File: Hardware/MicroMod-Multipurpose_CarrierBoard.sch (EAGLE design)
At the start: 83 parts, among them J11 microSD, J12 SPI, J14 I2C, J3 JTAG, J5 UART, J6 MICROMOD-2222-C, J8 Dedicated, Q2 600mA/40V, U1 S25FL127SABMFI100, U2 MCP73831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

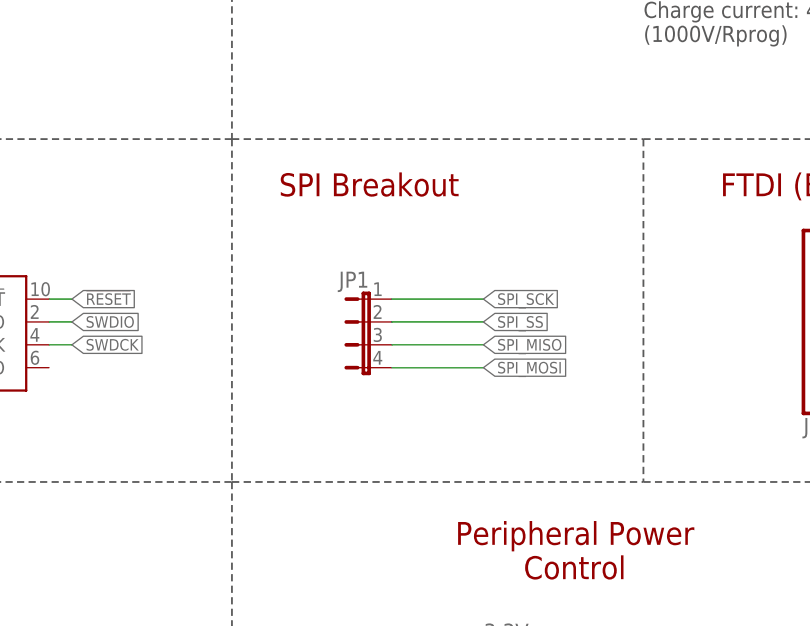
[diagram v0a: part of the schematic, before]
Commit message: FIX: Flash memory SPI breakout
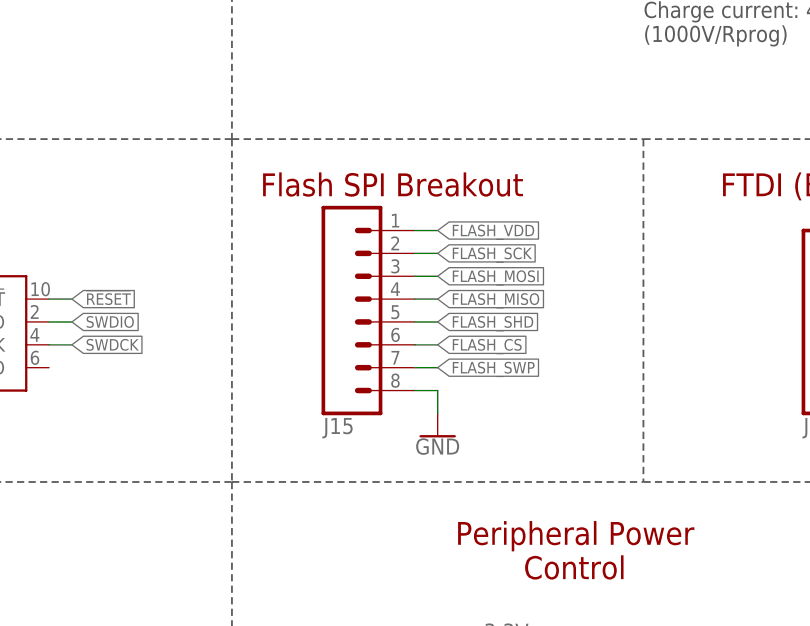
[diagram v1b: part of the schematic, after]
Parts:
- removed JP1: (no value), jumper:JP4E
- added J15: (no value), SparkFun-Connectors:CONN_08"
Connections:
- removed net SPI_MISO: JP1.3
- removed net SPI_MOSI: JP1.4
- removed net SPI_SS: JP1.2
- net FLASH_CS: now also J15.6
- net FLASH_MISO: now also J15.4
- net FLASH_MOSI: now also J15.3
- net FLASH_SCK: now also J15.2
- net FLASH_SHD: now also J15.5
- net FLASH_SWP: now also J15.7
- net FLASH_VDD: now also J15.1
- net GND: now also J15.8
- net SPI_SCK: no longer JP1.1
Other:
- note added: "Flash SPI Breakout"
- note removed: "SPI Breakout"
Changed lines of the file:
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@@
 <part name="GND1" library="SparkFun-PowerSymbols" deviceset="GND" device=""/>
 <part name="GND2" library="SparkFun-PowerSymbols" deviceset="GND" device=""/>
-<part name="JP1" library="jumper" library_urn="urn:adsk.eagle:library:252" deviceset="JP4E" device="" package3d_urn="urn:adsk.eagle:package:15463/1"/>
 <part name="J2" library="SparkFun-Connectors" library_urn="urn:adsk.eagle:library:513" deviceset="CONN_07" device="" package3d_urn="urn:adsk.eagle:package:38129/1"/>
 <part name="GND5" library="SparkFun-PowerSymbols" deviceset="GND" device=""/>
@@
 <part name="H3" library="SparkFun-Hardware" library_urn="urn:adsk.eagle:library:519" deviceset="STAND-OFF" device="" package3d_urn="urn:adsk.eagle:package:38630/1"/>
 <part name="H4" library="SparkFun-Hardware" library_urn="urn:adsk.eagle:library:519" deviceset="STAND-OFF" device="" package3d_urn="urn:adsk.eagle:package:38630/1"/>
+<part name="J15" library="SparkFun-Connectors" library_urn="urn:adsk.eagle:library:513" deviceset="CONN_08" device="&quot;" package3d_urn="urn:adsk.eagle:package:38138/1"/>
+<part name="GND36" library="SparkFun-PowerSymbols" deviceset="GND" device=""/>
 </parts>
 <sheets>
@@
 <wire x1="287.02" y1="0" x2="289.56" y2="0" width="0.2" layer="97" style="longdash"/>
 <wire x1="287.02" y1="144.78" x2="332.74" y2="144.78" width="0.2032" layer="97" style="longdash"/>
-<text x="302.26" y="139.7" size="2.54" layer="94" align="center">SPI Breakout</text>
+<text x="304.8" y="139.7" size="2.54" layer="94" align="center">Flash SPI Breakout</text>
 <wire x1="287.02" y1="106.68" x2="332.74" y2="106.68" width="0.2032" layer="97" style="longdash"/>
 <text x="325.12" y="99.06" size="2.54" layer="94" align="center">Peripheral Power
@@
 <attribute name="VALUE" x="35.56" y="131.826" size="1.778" layer="96" align="top-center"/>
 </instance>
-<instance part="JP1" gate="G$1" x="302.26" y="124.46" smashed="yes" rot="MR270">
-<attribute name="NAME" x="302.26" y="128.27" size="1.778" layer="95" rot="MR0"/>
-<attribute name="VALUE" x="302.26" y="116.205" size="1.778" layer="96" rot="MR0"/>
-</instance>
 <instance part="J2" gate="G$1" x="355.6" y="127" smashed="yes" rot="MR180">
 <attribute name="VALUE" x="350.52" y="136.906" size="1.778" layer="96" font="vector" rot="MR180"/>
@@
 <instance part="H3" gate="G$1" x="411.48" y="25.4" smashed="yes"/>
 <instance part="H4" gate="G$1" x="408.94" y="25.4" smashed="yes"/>
+<instance part="J15" gate="G$1" x="302.26" y="127" smashed="yes" rot="MR180">
+<attribute name="VALUE" x="297.18" y="139.446" size="1.778" layer="96" font="vector" rot="MR180"/>
+<attribute name="NAME" x="297.18" y="113.792" size="1.778" layer="95" font="vector" rot="MR180"/>
+</instance>
+<instance part="GND36" gate="1" x="309.88" y="111.76" smashed="yes" rot="MR0">
+<attribute name="VALUE" x="309.88" y="111.506" size="1.778" layer="96" rot="MR0" align="top-center"/>
+</instance>
 </instances>
 <busses>
@@
 <wire x1="243.84" y1="119.38" x2="241.3" y2="119.38" width="0.1524" layer="91"/>
 <pinref part="J3" gate="G$1" pin="GND"/>
+</segment>
+<segment>
+<pinref part="J15" gate="G$1" pin="8"/>
+<wire x1="307.34" y1="116.84" x2="309.88" y2="116.84" width="0.1524" layer="91"/>
+<pinref part="GND36" gate="1" pin="GND"/>
+<wire x1="309.88" y1="116.84" x2="309.88" y2="114.3" width="0.1524" layer="91"/>
 </segment>
 </net>
@@
 </segment>
 <segment>
-<pinref part="JP1" gate="G$1" pin="1"/>
-<wire x1="304.8" y1="127" x2="314.96" y2="127" width="0.1524" layer="91"/>
-<label x="314.96" y="127" size="1.27" layer="95" font="vector" xref="yes"/>
-</segment>
-<segment>
 <pinref part="J6" gate="J1" pin="SPI_SCK"/>
 <wire x1="208.28" y1="93.98" x2="210.82" y2="93.98" width="0.1524" layer="91"/>
@@
 <label x="210.82" y="25.4" size="1.27" layer="95" font="vector" xref="yes"/>
 </segment>
+<segment>
+<pinref part="J15" gate="G$1" pin="7"/>
+<wire x1="307.34" y1="119.38" x2="309.88" y2="119.38" width="0.1524" layer="91"/>
+<label x="309.88" y="119.38" size="1.27" layer="95" font="vector" xref="yes"/>
+</segment>
 </net>
 <net name="FLASH_SHD" class="0">
@@
 <wire x1="208.28" y1="27.94" x2="210.82" y2="27.94" width="0.1524" layer="91"/>
 <label x="210.82" y="27.94" size="1.27" layer="95" font="vector" xref="yes"/>
+</segment>
+<segment>
+<pinref part="J15" gate="G$1" pin="5"/>
+<wire x1="307.34" y1="124.46" x2="309.88" y2="124.46" width="0.1524" layer="91"/>
+<label x="309.88" y="124.46" size="1.27" layer="95" font="vector" xref="yes"/>
 </segment>
 </net>
@@
 <label x="383.54" y="254" size="1.27" layer="95" font="vector" xref="yes"/>
 </segment>
-</net>
-<net name="SPI_SS" class="0">
-<segment>
-<pinref part="JP1" gate="G$1" pin="2"/>
-<wire x1="304.8" y1="124.46" x2="314.96" y2="124.46" width="0.1524" layer="91"/>
-<label x="314.96" y="124.46" size="1.27" layer="95" font="vector" xref="yes"/>
-</segment>
-</net>
-<net name="SPI_MISO" class="0">
-<segment>
-<pinref part="JP1" gate="G$1" pin="3"/>
-<wire x1="304.8" y1="121.92" x2="314.96" y2="121.92" width="0.1524" layer="91"/>
-<label x="314.96" y="121.92" size="1.27" layer="95" font="vector" xref="yes"/>
-</segment>
-</net>
-<net name="SPI_MOSI" class="0">
-<segment>
-<pinref part="JP1" gate="G$1" pin="4"/>
-<wire x1="304.8" y1="119.38" x2="314.96" y2="119.38" width="0.1524" layer="91"/>
-<label x="314.96" y="119.38" size="1.27" layer="95" font="vector" xref="yes"/>
+<segment>
+<pinref part="J15" gate="G$1" pin="1"/>
+<wire x1="307.34" y1="134.62" x2="309.88" y2="134.62" width="0.1524" layer="91"/>
+<label x="309.88" y="134.62" size="1.27" layer="95" font="vector" xref="yes"/>
 </segment>
 </net>
@@
 <wire x1="208.28" y1="99.06" x2="210.82" y2="99.06" width="0.1524" layer="91"/>
 <label x="210.82" y="99.06" size="1.27" layer="95" font="vector" xref="yes"/>
+</segment>
+<segment>
+<pinref part="J15" gate="G$1" pin="6"/>
+<wire x1="307.34" y1="121.92" x2="309.88" y2="121.92" width="0.1524" layer="91"/>
+<label x="309.88" y="121.92" size="1.27" layer="95" font="vector" xref="yes"/>
 </segment>
 </net>
@@
 <label x="210.82" y="111.76" size="1.27" layer="95" font="vector" xref="yes"/>
 </segment>
+<segment>
+<pinref part="J15" gate="G$1" pin="2"/>
+<wire x1="307.34" y1="132.08" x2="309.88" y2="132.08" width="0.1524" layer="91"/>
+<label x="309.88" y="132.08" size="1.27" layer="95" font="vector" xref="yes"/>
+</segment>
 </net>
 <net name="FLASH_MOSI" class="0">
@@
 <wire x1="208.28" y1="109.22" x2="210.82" y2="109.22" width="0.1524" layer="91"/>
 <label x="210.82" y="109.22" size="1.27" layer="95" font="vector" xref="yes"/>
+</segment>
+<segment>
+<pinref part="J15" gate="G$1" pin="3"/>
+<wire x1="307.34" y1="129.54" x2="309.88" y2="129.54" width="0.1524" layer="91"/>
+<label x="309.88" y="129.54" size="1.27" layer="95" font="vector" xref="yes"/>
 </segment>
 </net>
@@
 <label x="210.82" y="106.68" size="1.27" layer="95" font="vector" xref="yes"/>
 </segment>
-</net>
+<segment>
+<pinref part="J15" gate="G$1" pin="4"/>
+<wire x1="307.34" y1="127" x2="309.88" y2="127" width="0.1524" layer="91"/>
+<label x="309.88" y="127" size="1.27" layer="95" font="vector" xref="yes"/>
+</segment>
+</net>

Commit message: Wire I2C_SCL1/SDA1 and G4-G11 as breakout GPIO pins
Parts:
- added J16: General GPIO, SparkFun-Connectors:CONN_08"
- added J17: I2C1, SparkFun-Connectors:I2C_STANDARD_NO_SILK
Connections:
- new net G10: J16.7, J6.G10/ADC_D+/CAM_VSYNC
- new net G11: J16.8, J6.G11
- new net G4: J16.1, J6.G4/BUS4
- new net G5: J16.2, J6.G5/BUS5
- new net G6: J16.3, J6.G6/BUS6
- new net G7: J16.4, J6.G7/BUS7
- new net G8: J16.5, J6.G8
- new net G9: J16.6, J6.G9/ADC_D-/CAM_HSYNC
- new net I2C_SCL1: J17.4, J6.I2C_SCL1
- new net I2C_SDA1: J17.3, J6.I2C_SDA1
- net 3.3V_LP: now also J17.2
- net FLASH_SHD: now also J6.G2/BUS2; no longer J6.G7/BUS7
- net FLASH_SWP: now also J6.G3/BUS3; no longer J6.G8
- net GND: now also J17.1
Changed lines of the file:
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@@
 <part name="J15" library="SparkFun-Connectors" library_urn="urn:adsk.eagle:library:513" deviceset="CONN_08" device="&quot;" package3d_urn="urn:adsk.eagle:package:38138/1"/>
 <part name="GND36" library="SparkFun-PowerSymbols" deviceset="GND" device=""/>
+<part name="J16" library="SparkFun-Connectors" library_urn="urn:adsk.eagle:library:513" deviceset="CONN_08" device="&quot;" package3d_urn="urn:adsk.eagle:package:38138/1" value="General GPIO"/>
+<part name="J17" library="SparkFun-Connectors" deviceset="I2C_STANDARD" device="_NO_SILK" value="I2C1"/>
+<part name="GND37" library="SparkFun-PowerSymbols" deviceset="GND" device=""/>
 </parts>
 <sheets>
@@
 <attribute name="VALUE" x="309.88" y="111.506" size="1.778" layer="96" rot="MR0" align="top-center"/>
 </instance>
+<instance part="J16" gate="G$1" x="78.74" y="78.74" smashed="yes" rot="MR180">
+<attribute name="VALUE" x="73.66" y="91.186" size="1.778" layer="96" font="vector" rot="MR180"/>
+<attribute name="NAME" x="73.66" y="65.532" size="1.778" layer="95" font="vector" rot="MR180"/>
+</instance>
+<instance part="J17" gate="G$1" x="109.22" y="12.7" smashed="yes" rot="MR0">
+<attribute name="VALUE" x="108.458" y="20.828" size="1.778" layer="96" font="vector" rot="MR180" align="top-left"/>
+<attribute name="NAME" x="107.95" y="5.334" size="1.778" layer="95" font="vector"/>
+</instance>
+<instance part="GND37" gate="1" x="99.06" y="5.08" smashed="yes">
+<attribute name="VALUE" x="99.06" y="4.826" size="1.778" layer="96" align="top-center"/>
+</instance>
 </instances>
 <busses>
@@
 <pinref part="GND36" gate="1" pin="GND"/>
 <wire x1="309.88" y1="116.84" x2="309.88" y2="114.3" width="0.1524" layer="91"/>
+</segment>
+<segment>
+<pinref part="J17" gate="G$1" pin="1"/>
+<wire x1="101.6" y1="10.16" x2="99.06" y2="10.16" width="0.1524" layer="91"/>
+<pinref part="GND37" gate="1" pin="GND"/>
+<wire x1="99.06" y1="10.16" x2="99.06" y2="7.62" width="0.1524" layer="91"/>
 </segment>
 </net>
@@
 <label x="45.72" y="48.26" size="1.27" layer="95" rot="R90" xref="yes"/>
 </segment>
+<segment>
+<pinref part="J17" gate="G$1" pin="2"/>
+<wire x1="101.6" y1="12.7" x2="99.06" y2="12.7" width="0.1524" layer="91"/>
+<wire x1="99.06" y1="12.7" x2="99.06" y2="20.32" width="0.1524" layer="91"/>
+<label x="99.06" y="20.32" size="1.27" layer="95" rot="R90" xref="yes"/>
+</segment>
 </net>
 <net name="FLASH_SWP" class="0">
@@
 </segment>
 <segment>
-<pinref part="J6" gate="J1" pin="G8"/>
-<wire x1="208.28" y1="25.4" x2="210.82" y2="25.4" width="0.1524" layer="91"/>
-<label x="210.82" y="25.4" size="1.27" layer="95" font="vector" xref="yes"/>
-</segment>
-<segment>
 <pinref part="J15" gate="G$1" pin="7"/>
 <wire x1="307.34" y1="119.38" x2="309.88" y2="119.38" width="0.1524" layer="91"/>
 <label x="309.88" y="119.38" size="1.27" layer="95" font="vector" xref="yes"/>
 </segment>
+<segment>
+<pinref part="J6" gate="J1" pin="G3/BUS3"/>
+<wire x1="208.28" y1="38.1" x2="210.82" y2="38.1" width="0.1524" layer="91"/>
+<label x="210.82" y="38.1" size="1.27" layer="95" font="vector" xref="yes"/>
+</segment>
 </net>
 <net name="FLASH_SHD" class="0">
@@
 </segment>
 <segment>
-<pinref part="J6" gate="J1" pin="G7/BUS7"/>
-<wire x1="208.28" y1="27.94" x2="210.82" y2="27.94" width="0.1524" layer="91"/>
-<label x="210.82" y="27.94" size="1.27" layer="95" font="vector" xref="yes"/>
-</segment>
-<segment>
 <pinref part="J15" gate="G$1" pin="5"/>
 <wire x1="307.34" y1="124.46" x2="309.88" y2="124.46" width="0.1524" layer="91"/>
 <label x="309.88" y="124.46" size="1.27" layer="95" font="vector" xref="yes"/>
+</segment>
+<segment>
+<pinref part="J6" gate="J1" pin="G2/BUS2"/>
+<wire x1="208.28" y1="40.64" x2="210.82" y2="40.64" width="0.1524" layer="91"/>
+<label x="210.82" y="40.64" size="1.27" layer="95" font="vector" xref="yes"/>
 </segment>
 </net>
@@
 </segment>
 </net>
+<net name="G4" class="0">
+<segment>
+<pinref part="J6" gate="J1" pin="G4/BUS4"/>
+<wire x1="208.28" y1="35.56" x2="210.82" y2="35.56" width="0.1524" layer="91"/>
+<label x="210.82" y="35.56" size="1.27" layer="95" font="vector" xref="yes"/>
+</segment>
+<segment>
+<pinref part="J16" gate="G$1" pin="1"/>
+<wire x1="83.82" y1="86.36" x2="86.36" y2="86.36" width="0.1524" layer="91"/>
+<label x="86.36" y="86.36" size="1.27" layer="95" font="vector" xref="yes"/>
+</segment>
+</net>
+<net name="G5" class="0">
+<segment>
+<pinref part="J6" gate="J1" pin="G5/BUS5"/>
+<wire x1="208.28" y1="33.02" x2="210.82" y2="33.02" width="0.1524" layer="91"/>
+<label x="210.82" y="33.02" size="1.27" layer="95" font="vector" xref="yes"/>
+</segment>
+<segment>
+<pinref part="J16" gate="G$1" pin="2"/>
+<wire x1="83.82" y1="83.82" x2="86.36" y2="83.82" width="0.1524" layer="91"/>
+<label x="86.36" y="83.82" size="1.27" layer="95" font="vector" xref="yes"/>
+</segment>
+</net>
+<net name="G6" class="0">
+<segment>
+<pinref part="J6" gate="J1" pin="G6/BUS6"/>
+<wire x1="208.28" y1="30.48" x2="210.82" y2="30.48" width="0.1524" layer="91"/>
+<label x="210.82" y="30.48" size="1.27" layer="95" font="vector" xref="yes"/>
+</segment>
+<segment>
+<pinref part="J16" gate="G$1" pin="3"/>
+<wire x1="83.82" y1="81.28" x2="86.36" y2="81.28" width="0.1524" layer="91"/>
+<label x="86.36" y="81.28" size="1.27" layer="95" font="vector" xref="yes"/>
+</segment>
+</net>
+<net name="G7" class="0">
+<segment>
+<pinref part="J6" gate="J1" pin="G7/BUS7"/>
+<wire x1="208.28" y1="27.94" x2="210.82" y2="27.94" width="0.1524" layer="91"/>
+<label x="210.82" y="27.94" size="1.27" layer="95" font="vector" xref="yes"/>
+</segment>
+<segment>
+<pinref part="J16" gate="G$1" pin="4"/>
+<wire x1="83.82" y1="78.74" x2="86.36" y2="78.74" width="0.1524" layer="91"/>
+<label x="86.36" y="78.74" size="1.27" layer="95" font="vector" xref="yes"/>
+</segment>
+</net>
+<net name="G8" class="0">
+<segment>
+<pinref part="J6" gate="J1" pin="G8"/>
+<wire x1="208.28" y1="25.4" x2="210.82" y2="25.4" width="0.1524" layer="91"/>
+<label x="210.82" y="25.4" size="1.27" layer="95" font="vector" xref="yes"/>
+</segment>
+<segment>
+<pinref part="J16" gate="G$1" pin="5"/>
+<wire x1="83.82" y1="76.2" x2="86.36" y2="76.2" width="0.1524" layer="91"/>
+<label x="86.36" y="76.2" size="1.27" layer="95" font="vector" xref="yes"/>
+</segment>
+</net>
+<net name="G9" class="0">
+<segment>
+<pinref part="J6" gate="J1" pin="G9/ADC_D-/CAM_HSYNC"/>
+<wire x1="208.28" y1="22.86" x2="210.82" y2="22.86" width="0.1524" layer="91"/>
+<label x="210.82" y="22.86" size="1.27" layer="95" font="vector" xref="yes"/>
+</segment>
+<segment>
+<pinref part="J16" gate="G$1" pin="6"/>
+<wire x1="83.82" y1="73.66" x2="86.36" y2="73.66" width="0.1524" layer="91"/>
+<label x="86.36" y="73.66" size="1.27" layer="95" font="vector" xref="yes"/>
+</segment>
+</net>
+<net name="G10" class="0">
+<segment>
+<pinref part="J6" gate="J1" pin="G10/ADC_D+/CAM_VSYNC"/>
+<wire x1="208.28" y1="20.32" x2="210.82" y2="20.32" width="0.1524" layer="91"/>
+<label x="210.82" y="20.32" size="1.27" layer="95" font="vector" xref="yes"/>
+</segment>
+<segment>
+<pinref part="J16" gate="G$1" pin="7"/>
+<wire x1="83.82" y1="71.12" x2="86.36" y2="71.12" width="0.1524" layer="91"/>
+<label x="86.36" y="71.12" size="1.27" layer="95" font="vector" xref="yes"/>
+</segment>
+</net>
+<net name="G11" class="0">
+<segment>
+<pinref part="J6" gate="J1" pin="G11"/>
+<wire x1="208.28" y1="17.78" x2="210.82" y2="17.78" width="0.1524" layer="91"/>
+<label x="210.82" y="17.78" size="1.27" layer="95" font="vector" xref="yes"/>
+</segment>
+<segment>
+<pinref part="J16" gate="G$1" pin="8"/>
+<wire x1="83.82" y1="68.58" x2="86.36" y2="68.58" width="0.1524" layer="91"/>
+<label x="86.36" y="68.58" size="1.27" layer="95" font="vector" xref="yes"/>
+</segment>
+</net>
+<net name="I2C_SCL1" class="0">
+<segment>
+<pinref part="J6" gate="J1" pin="I2C_SCL1"/>
+<wire x1="162.56" y1="38.1" x2="160.02" y2="38.1" width="0.1524" layer="91"/>
+<label x="160.02" y="38.1" size="1.27" layer="95" rot="R180" xref="yes"/>
+</segment>
+<segment>
+<pinref part="J17" gate="G$1" pin="4"/>
+<wire x1="101.6" y1="17.78" x2="96.52" y2="17.78" width="0.1524" layer="91"/>
+<label x="96.52" y="17.78" size="1.27" layer="95" rot="R180" xref="yes"/>
+</segment>
+</net>
+<net name="I2C_SDA1" class="0">
+<segment>
+<pinref part="J6" gate="J1" pin="I2C_SDA1"/>
+<wire x1="162.56" y1="35.56" x2="160.02" y2="35.56" width="0.1524" layer="91"/>
+<label x="160.02" y="35.56" size="1.27" layer="95" rot="R180" xref="yes"/>
+</segment>
+<segment>
+<pinref part="J17" gate="G$1" pin="3"/>
+<wire x1="101.6" y1="15.24" x2="96.52" y2="15.24" width="0.1524" layer="91"/>
+<label x="96.52" y="15.24" size="1.27" layer="95" rot="R180" xref="yes"/>
+</segment>
+</net>
